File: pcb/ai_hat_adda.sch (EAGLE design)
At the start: 48 parts, among them J1 1X03ST, J2 1X03ST, J3 1X02ST, J4 1X02ST, K1 2X20-RPI, U1 24LC32A, U2 ADS1115, U3 MCP4725, U4 MCP4725

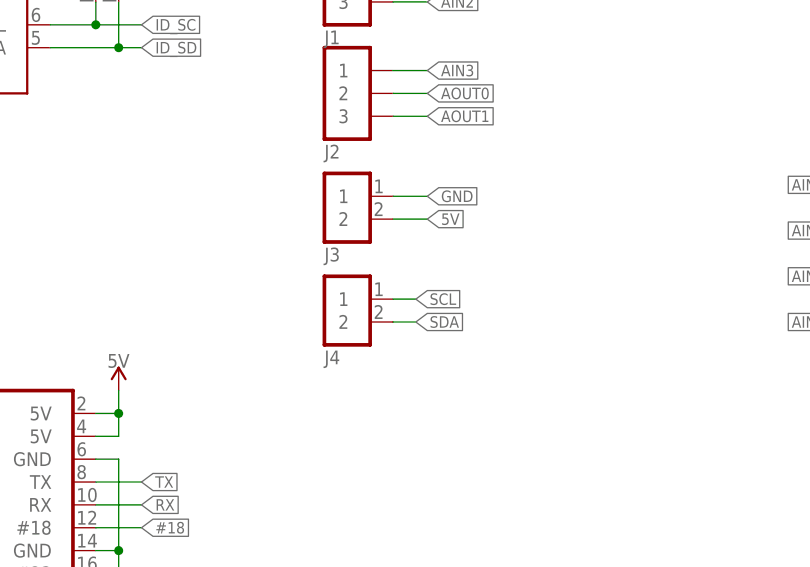
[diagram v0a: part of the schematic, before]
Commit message: minor silkscreen updates. added 3V3 output.
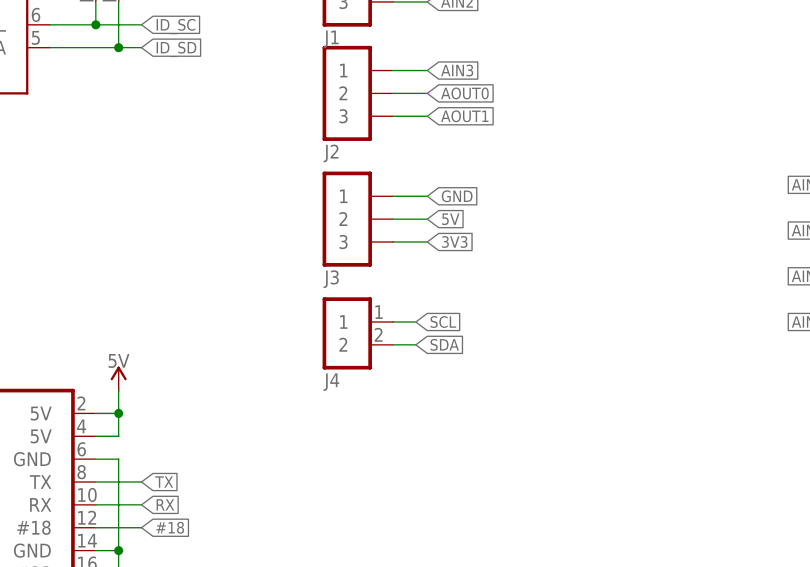
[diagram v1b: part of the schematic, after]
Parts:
- J3: value 1X02ST -> 1X03ST; device Ai_Connectors:1X02ST -> Ai_Connectors:1X03ST
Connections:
- net 3V3: now also J3.3
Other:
- moved on the sheet: J3, J4
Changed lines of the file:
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@@
 <?xml version="1.0" encoding="utf-8"?>
 <!DOCTYPE eagle SYSTEM "eagle.dtd">
-<eagle version="7.2.0">
+<eagle version="7.1.0">
 <drawing>
 <settings>
@@
 <part name="J1" library="Ai_Connectors" deviceset="1X03" device="ST"/>
 <part name="J2" library="Ai_Connectors" deviceset="1X03" device="ST"/>
-<part name="J3" library="Ai_Connectors" deviceset="1X02" device="ST"/>
 <part name="J4" library="Ai_Connectors" deviceset="1X02" device="ST"/>
+<part name="J3" library="Ai_Connectors" deviceset="1X03" device="ST"/>
 </parts>
 <sheets>
@@
 <instance part="J1" gate="G$1" x="63.5" y="162.56" rot="MR180"/>
 <instance part="J2" gate="G$1" x="63.5" y="149.86" rot="MR180"/>
+<instance part="J4" gate="G$1" x="63.5" y="121.92" rot="MR180"/>
 <instance part="J3" gate="G$1" x="63.5" y="135.89" rot="MR180"/>
-<instance part="J4" gate="G$1" x="63.5" y="124.46" rot="MR180"/>
 </instances>
 <busses>
@@
 </segment>
 <segment>
-<pinref part="J3" gate="G$1" pin="1"/>
 <wire x1="68.58" y1="138.43" x2="72.39" y2="138.43" width="0.1524" layer="91"/>
 <label x="72.39" y="138.43" size="1.27" layer="95" font="vector" ratio="10" xref="yes"/>
+<pinref part="J3" gate="G$1" pin="1"/>
 </segment>
 <segment>
@@
 </segment>
 <segment>
-<pinref part="J3" gate="G$1" pin="2"/>
 <wire x1="68.58" y1="135.89" x2="72.39" y2="135.89" width="0.1524" layer="91"/>
 <label x="72.39" y="135.89" size="1.27" layer="95" font="vector" ratio="10" xref="yes"/>
+<pinref part="J3" gate="G$1" pin="2"/>
 </segment>
 </net>
@@
 <junction x="160.02" y="165.1"/>
 </segment>
+<segment>
+<pinref part="J3" gate="G$1" pin="3"/>
+<wire x1="68.58" y1="133.35" x2="72.39" y2="133.35" width="0.1524" layer="91"/>
+<label x="72.39" y="133.35" size="1.27" layer="95" font="vector" ratio="10" xref="yes"/>
+</segment>
 </net>
 <net name="ID_SC" class="0">
@@
 <segment>
 <pinref part="J4" gate="G$1" pin="2"/>
-<wire x1="68.58" y1="124.46" x2="71.12" y2="124.46" width="0.1524" layer="91"/>
-<label x="71.12" y="124.46" size="1.27" layer="95" font="vector" ratio="10" xref="yes"/>
+<wire x1="68.58" y1="121.92" x2="71.12" y2="121.92" width="0.1524" layer="91"/>
+<label x="71.12" y="121.92" size="1.27" layer="95" font="vector" ratio="10" xref="yes"/>
 </segment>
 </net>
@@
 <segment>
 <pinref part="J4" gate="G$1" pin="1"/>
-<wire x1="68.58" y1="127" x2="71.12" y2="127" width="0.1524" layer="91"/>
-<label x="71.12" y="127" size="1.27" layer="95" font="vector" ratio="10" xref="yes"/>
-</segment>
-</net>
+<wire x1="68.58" y1="124.46" x2="71.12" y2="124.46" width="0.1524" layer="91"/>
+<label x="71.12" y="124.46" size="1.27" layer="95" font="vector" ratio="10" xref="yes"/>
+</segment>
+</net>

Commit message: updating
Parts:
- K1: value 2X20-RPI -> 2X20-RPI-ALT; device Ai_Connectors:2X20-RPI -> Ai_Connectors:2X20-RPI-ALT
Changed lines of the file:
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@@
 </classes>
 <parts>
-<part name="K1" library="Ai_Connectors" deviceset="2X20-RPI" device=""/>
+<part name="K1" library="Ai_Connectors" deviceset="2X20-RPI" device="-ALT" value="2X20-RPI-ALT"/>
 <part name="U1" library="Ai_IC" deviceset="24LC32A" device=""/>
 <part name="GND10" library="Ai_Power" deviceset="GND" device=""/>

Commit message: updating
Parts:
- removed U1: 24LC32A, Ai_IC:24LC32A
- added EEPROM: 24LC32A, Ai_IC:24LC32A
- U3, U4: device SparkFun-AnalogIC:MCP4725SOT-23 -> Ai_IC:MCP4725SOT-23
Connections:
- net 3V3: now also EEPROM.VCC, R5.1; no longer U1.VCC
- net GND: now also EEPROM.A0, EEPROM.A1, EEPROM.A2, EEPROM.GND; no longer R5.1, U1.A0, U1.A1, U1.A2, U1.GND
- net ID_SC: now also EEPROM.SCL; no longer U1.SCL
- net ID_SD: now also EEPROM.SDA; no longer U1.SDA
- net N$2: now also U3.AO; no longer U4.AO
- net N$3: now also EEPROM.WP; no longer U1.WP
- net N$4: now also U4.AO; no longer U3.AO
- net SCL: now also J4.2; no longer J4.1
- net SDA: now also J4.1; no longer J4.2
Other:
- moved on the sheet: C1, C2, C3, C4, C5, CFG, J1, J2, J3, J4, K1, R1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

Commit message: updating
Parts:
- added FRAME1: FRAME-LETTER, Ai_Miscellany:FRAME-LETTER
- C1: value 100nF -> 0.1uF
- R1, R2: value 3k9 -> 3K9
- R3: value 1k -> 1K
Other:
- moved on the sheet: #12, #13, #15, #16, #17, #18, #20, #21, #22, #25, #27, #4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
